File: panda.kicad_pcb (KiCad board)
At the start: 2 copper layers, 100 x 125 mm, 154 parts, among them J1 PIN6-9_Breakout, J10 Screw_Terminal_01x02, J11 24V_Lockout_Key_Switch, J12 XT60-M, J13 PT_1, J14 PT_4, J15 PT_2, J16 PT_5, J17 PT_3, J18 PT_6, J19 4-Pin Load Cell, J2 PIN10-13_Breakout, J20 5-Pin Load Cell, J21 Ignitor Screw Terminal, J3 Valve_1_PWR, J4 Valve_4_PWR, J5 Valve_2_PWR, J6 Valve_5_PWR, J7 Valve_3_PWR, J8 Valve_6_PWR, J9 Screw_Terminal_01x04, K1 G5Q-1A DC24, K2 G5Q-1A DC24, Q1 BSS138, Q2 BSS138, Q3 BSS138, Q4 BSS138, Q5 BSS138, Q6 BSS138, Q7 BSS138, Q8 BSS138, U1 ESP32-S3, U2 ADS112C04, U3 ADS112C04, U4 ADS112C04, U5 ADS112C04, U6 XC6206P332MR, U8 TPS5430DDA

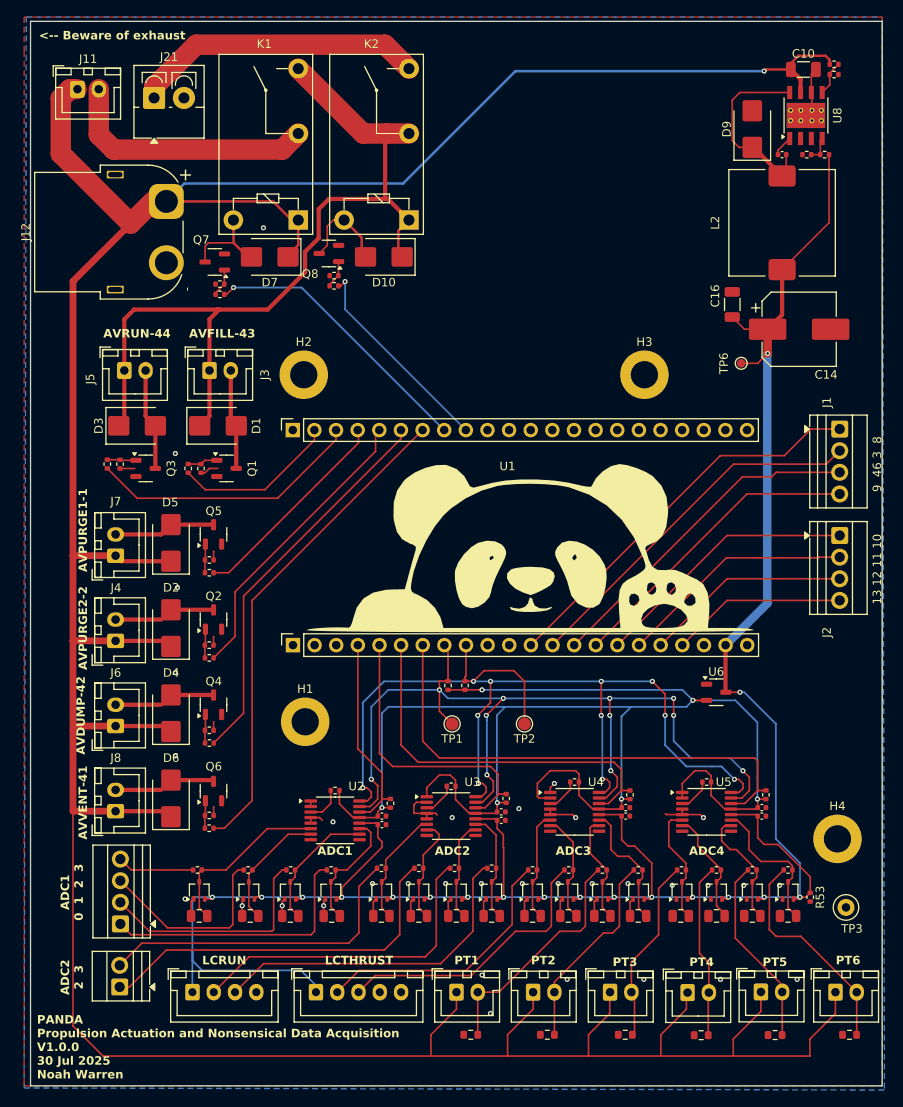
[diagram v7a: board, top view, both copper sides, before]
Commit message: Add current sensing and fuse mount for IGN
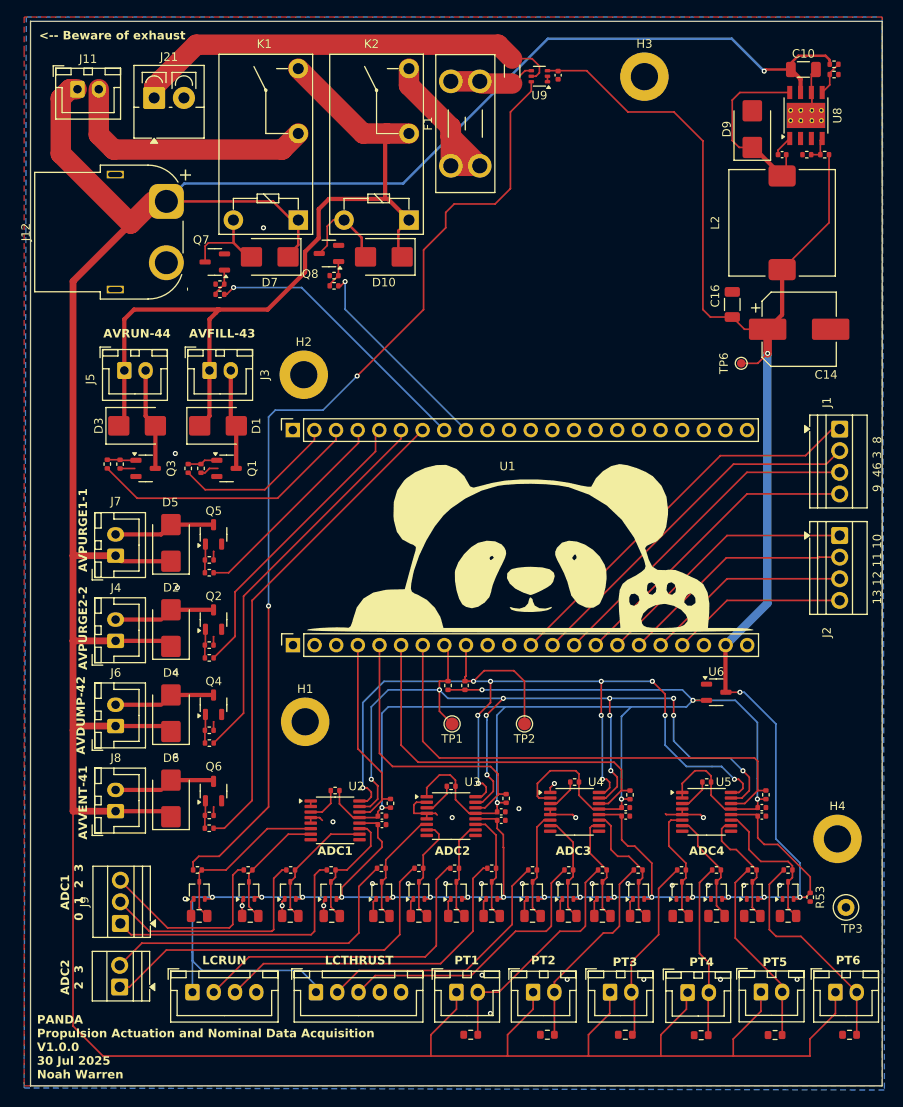
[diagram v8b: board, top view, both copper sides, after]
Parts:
- added C29: 0.1μF, Capacitor_SMD:C_0402_1005Metric, F.Cu at (172.2, 31.1)
- added F1: Fuse, Fuse:Fuseholder_Blade_Mini_Keystone_3568, F.Cu at (159.6, 41.7)
- added R54: 5m 1W, Resistor_SMD:R_1206_3216Metric, F.Cu at (166.8, 30.6)
- added U9: INA199A2DCK, Package_TO_SOT_SMD:SOT-363_SC-70-6, F.Cu at (170.0, 31.2)
- J9: value Screw_Terminal_01x04 -> Screw_Terminal_01x03; footprint TerminalBlock:TerminalBlock_Xinya_XY308-2.54-4P_1x04_P2.54mm_Horizontal -> TerminalBlock:TerminalBlock_Xinya_XY308-2.54-3P_1x03_P2.54mm_Horizontal
- moved H3 35.0 mm to (182.3, 31.2)
- moved J9 0.06 mm to (120.8, 130.7)
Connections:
- K2 pad 3: /Ignitor Control/IGNITOR_SOURCE -> Net-(F1-Pad1)
- R27 pad 1: Net-(J9-Pin_4) -> IGN_Current_Measurement
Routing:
- net IGN_Current_Measurement: track 0.00 -> 116.5 mm, vias 0 -> 2
- net +5V: track 275.2 -> 320.5 mm
- net Net-(F1-Pad1): track 0.00 -> 22.8 mm
- net /Ignitor Control/IGNITOR_SOURCE: track 34.4 -> 51.5 mm
- net Net-(U9-+): track 0.00 -> 10.2 mm
- net Net-(J9-Pin_4): track 9.07 -> 0.00 mm
- net +24V: track 418.9 -> 422.0 mm
- net GND: track 57.6 -> 58.3 mm
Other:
- board text added: "PANDA Propulsion Actuation and Nominal Data Acquisition V1.0.0 30 Jul 2025 Noah Warren"
- board text removed: "PANDA Propulsion Actuation and Nonsensical Data Acquisition V1.0.0 30 Jul 2025 Noah Warren"
